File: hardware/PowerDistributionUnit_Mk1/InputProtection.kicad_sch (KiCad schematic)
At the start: 22 parts, among them Q1 NVMFWS1D7N04XMT1G, U2 LM74502HDDFR

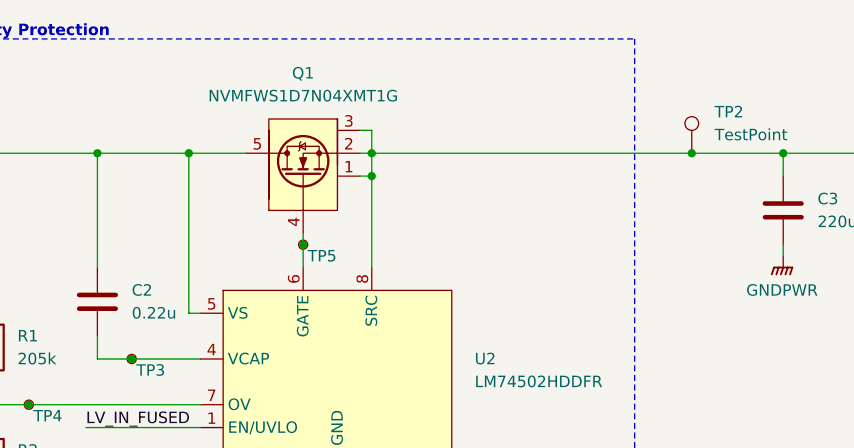
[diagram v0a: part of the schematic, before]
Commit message: make input protection use b2b FETs
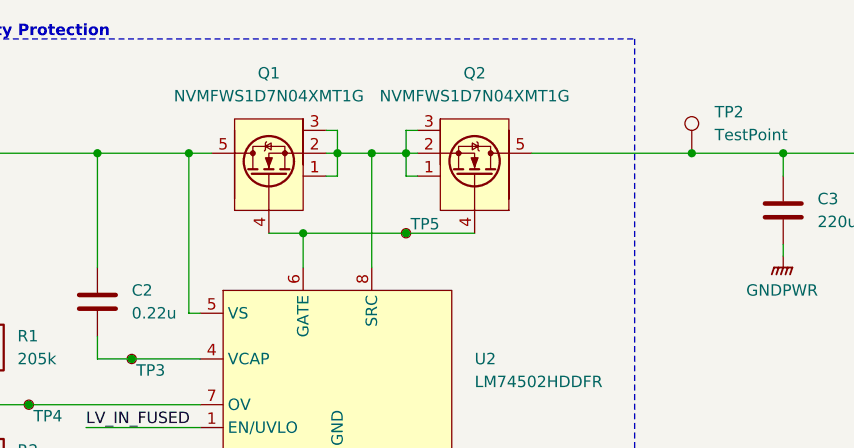
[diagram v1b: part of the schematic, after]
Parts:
- added Q2: NVMFWS1D7N04XMT1G, PowerDistributionUnitLib:NVMFWS1D7N04XMT1G, symbol PowerDistributionUnitLib:NVMFWS1D7N04XMT1G
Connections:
- net LV: now also Q2.5; no longer Q1.1, Q1.2, Q1.3, U2.8 (SRC)
- net at Q1.4, TP5.1, U2.6 (GATE): now also Q2.4
- new net: Q1.1, Q1.2, Q1.3, Q2.1, Q2.2, Q2.3, U2.8 (SRC)
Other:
- moved on the sheet: Q1, TP5
